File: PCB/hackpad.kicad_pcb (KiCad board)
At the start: 2 copper layers, 79 x 99 mm, 51 parts, among them J1 Conn_01x04, SW1 SW_Push, SW10 SW_Push, SW11 SW_Push, SW12 SW_Push, SW13 SW_Push, SW14 SW_Push, SW15 SW_Push, SW16 SW_Push, SW2 SW_Push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

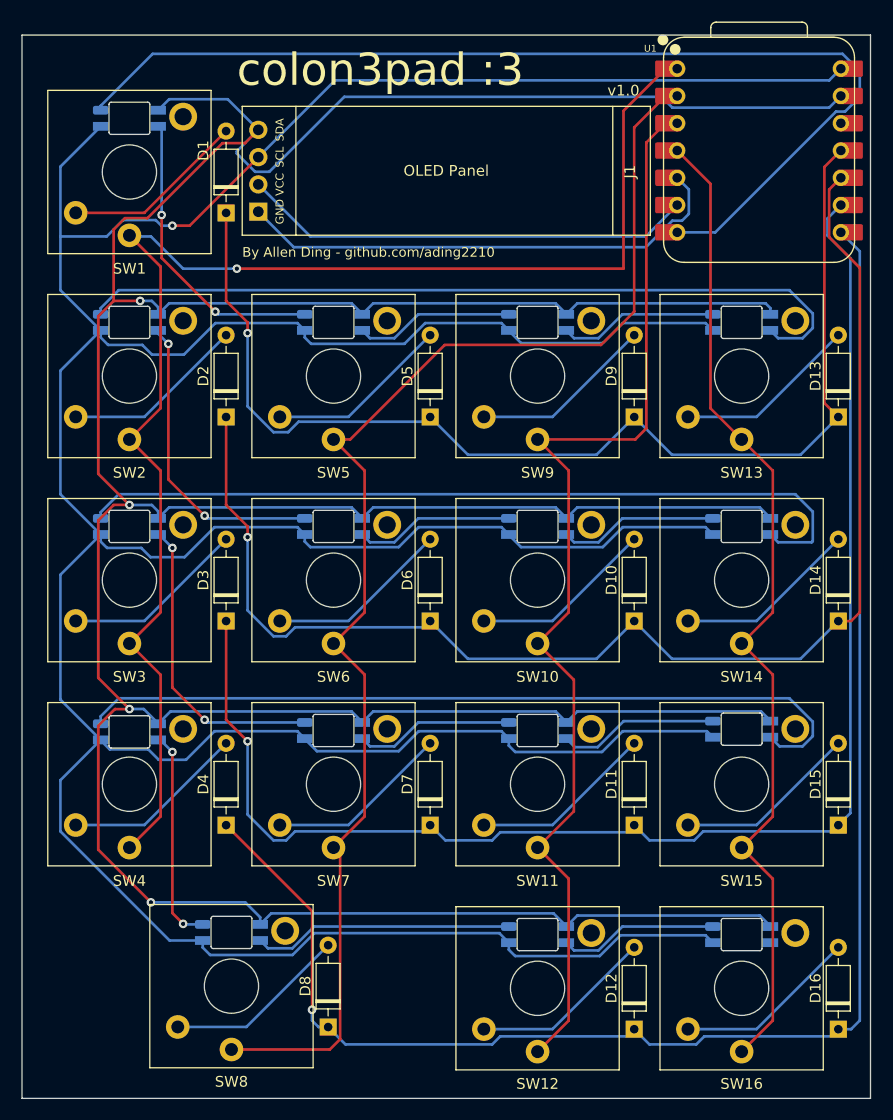
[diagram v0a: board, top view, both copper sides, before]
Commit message: finalize pcb traces and silkscreen text
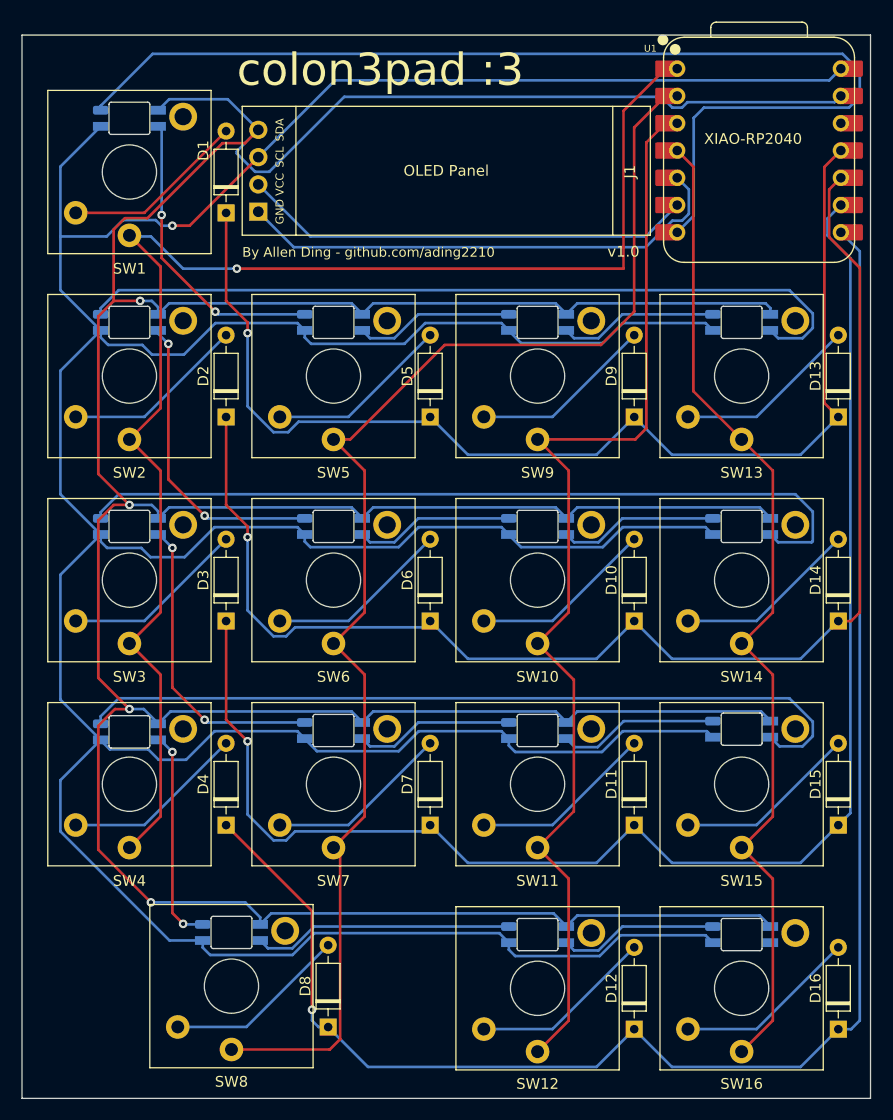
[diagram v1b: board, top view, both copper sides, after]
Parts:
- added G***: LOGO, LOGO, B.Cu at (141.5, 56.0)
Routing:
- net /DATA: track 98.4 -> 103.7 mm
- net /ROW3: track 137.4 -> 140.8 mm
- net /ROW4: track 149.6 -> 153.1 mm
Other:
- board text added: "Source code:"
- board text added: "XIAO-RP2040"

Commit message: add cutouts for key stabilizer
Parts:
- added Kailh PG1350: Choc, Keebio-Parts:Kailh-PG1350-Stab-Cutout, F.Cu at (92.5, 130.0)
- SW8: footprint Switch_Keyboard_Kailh:SW_Kailh_Choc_V2_1.00u -> Switch_Keyboard_Kailh:SW_Kailh_Choc_V2_2.00u
- moved D8 9.50 mm to (111.0, 133.8)
- moved SW8 0.20 mm to (92.5, 130.0)
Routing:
- net /COL2: track 126.7 -> 143.8 mm
- net Net-(D8-A): track 17.2 -> 26.7 mm
- net GND: track 415.5 -> 415.0 mm
- net /ROW4: track 153.1 -> 153.0 mm, vias 1 -> 0
